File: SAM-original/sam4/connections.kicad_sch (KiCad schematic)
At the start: 24 parts, among them J10 Conn_01x02_Socket, J11 Conn_01x02_Socket, J12 10103594-0001LF, J13 Conn_01x04_Socket, J14 Conn_01x04_Socket, J15 Conn_01x04_Socket, J16 Conn_01x04_Socket, J17 Conn_01x04_Socket, J6 XT60PW-M, J7 XT60PW-M, J8 XT30PW-F, J9 Conn_02x16_Odd_Even, SW1 SW_SPST

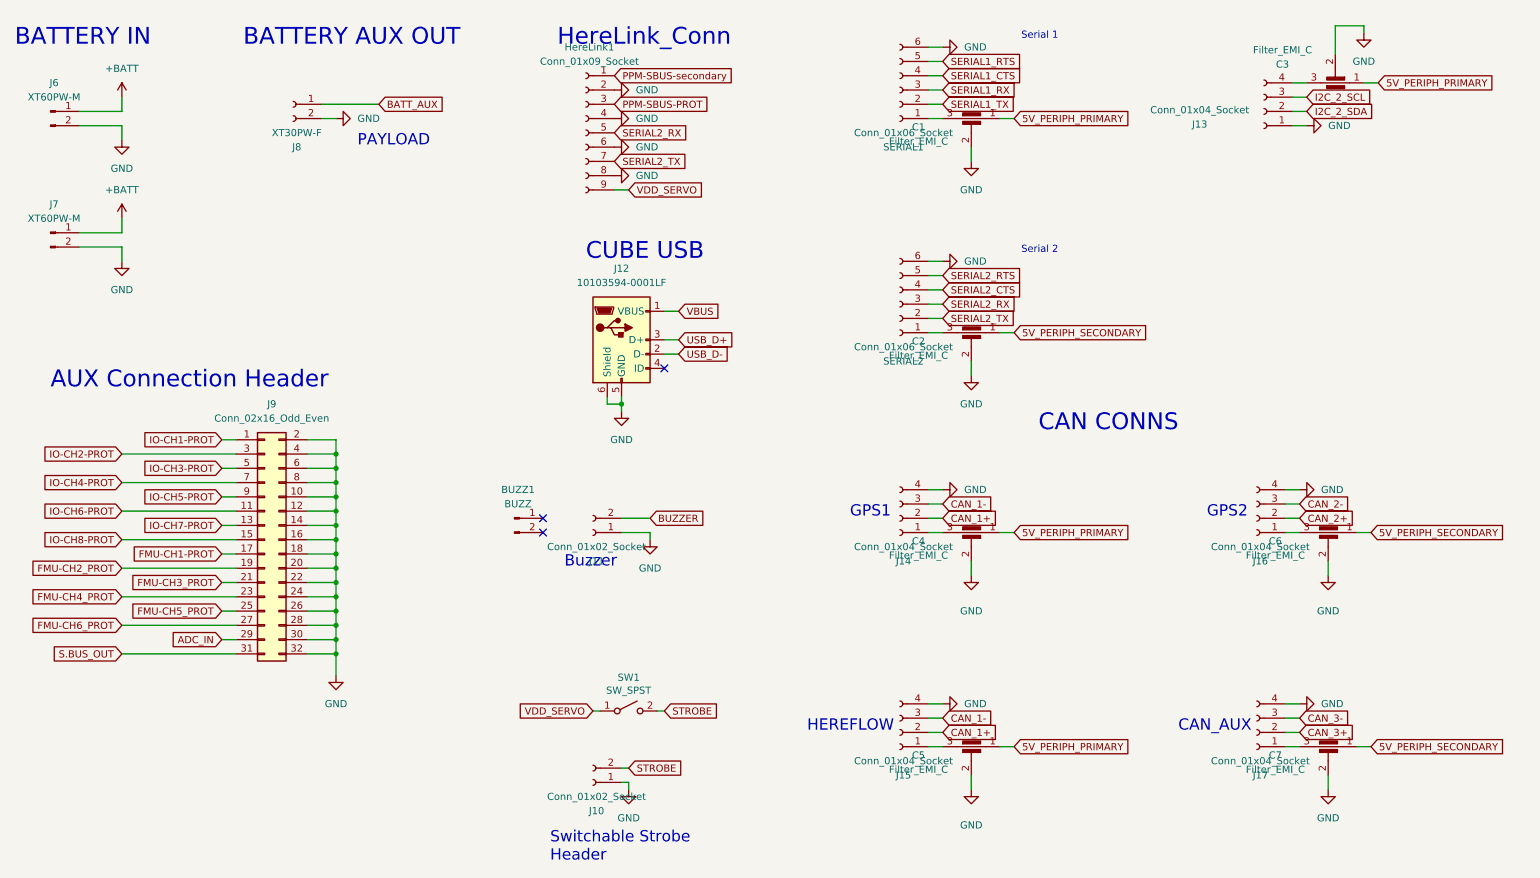
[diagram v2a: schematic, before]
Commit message: finalize core routing
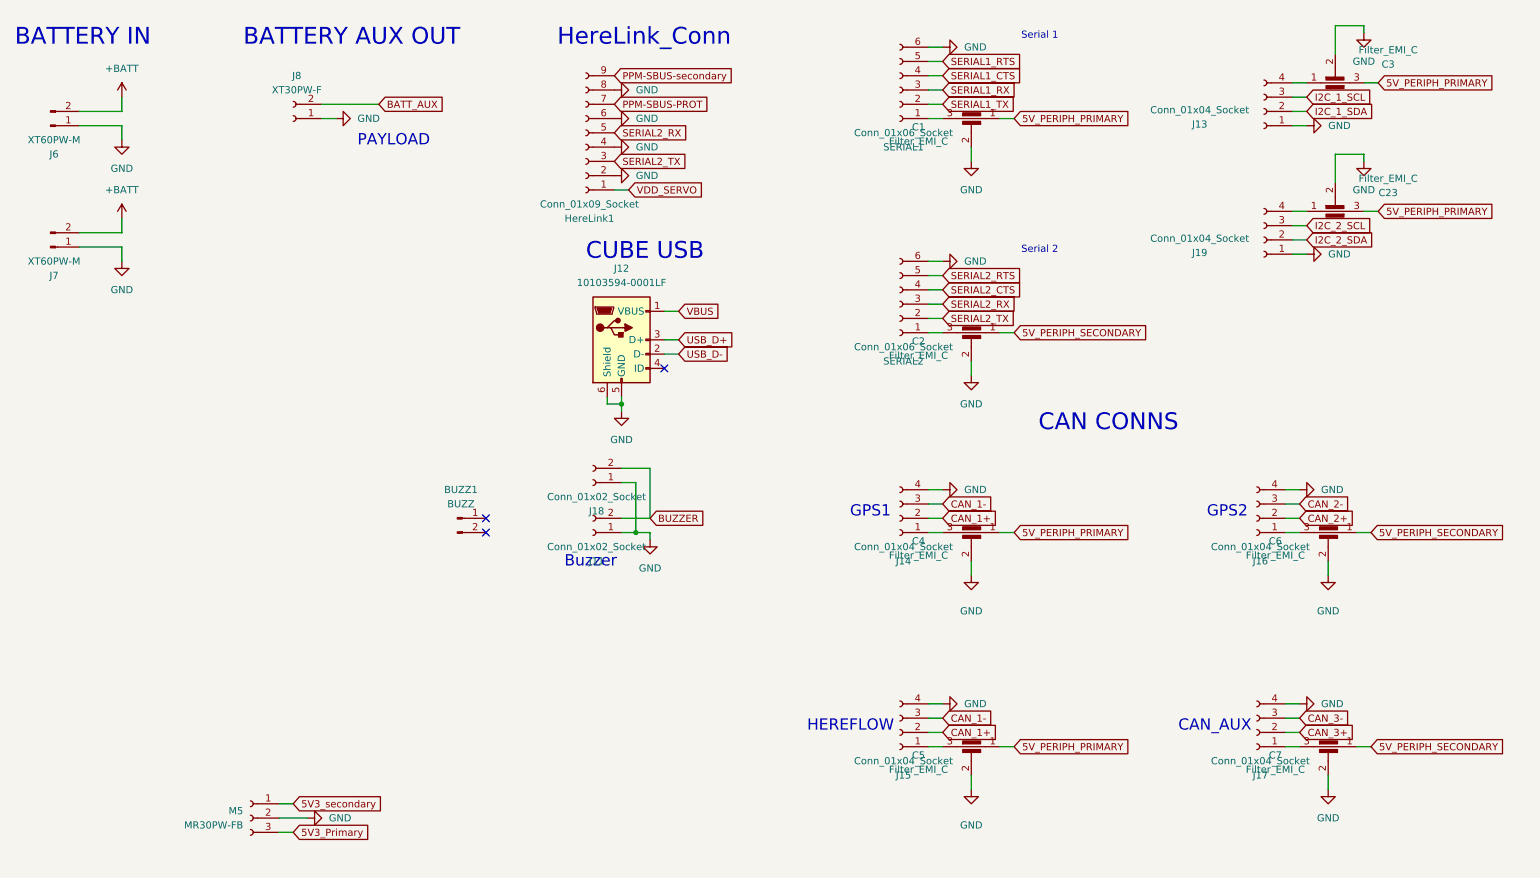
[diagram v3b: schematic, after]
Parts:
- removed J10: Conn_01x02_Socket, Connector_Molex:Molex_CLIK-Mate_502386-0270_1x02-1MP_P1.25mm_Horizontal, symbol Connector:Conn_01x02_Socket
- removed J9: Conn_02x16_Odd_Even, Connector_PinHeader_2.54mm:PinHeader_2x16_P2.54mm_Vertical, symbol Connector_Generic:Conn_02x16_Odd_Even
- removed SW1: SW_SPST, aerpaw-footprints:sam_slide_switch_5x5, symbol Switch:SW_SPST
- added C23: Filter_EMI_C, aerpaw-footprints:FIL_NFM21HC224R1A3D, symbol Device:Filter_EMI_C
- added J18: Conn_01x02_Socket, Connector_Molex:Molex_CLIK-Mate_502386-0270_1x02-1MP_P1.25mm_Horizontal, symbol Connector:Conn_01x02_Socket
- added J19: Conn_01x04_Socket, Connector_JST:JST_GH_BM04B-GHS-TBT_1x04-1MP_P1.25mm_Vertical, symbol Connector:Conn_01x04_Socket
- added M5: MR30PW-FB, Connector_AMASS:AMASS_MR30PW-FB_1x03_P3.50mm_Horizontal, symbol Connector:Conn_01x03_Socket
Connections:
- net +BATT: now also J6.2 (Pin_2), J7.2 (Pin_2); no longer J6.1 (Pin_1), J7.1 (Pin_1)
- net 5V_PERIPH_PRIMARY: now also C3.3, C23.3; no longer C3.1
- net BATT_AUX: now also J8.2 (Pin_2); no longer J8.1 (Pin_1)
- net BUZZER: now also J18.2 (Pin_2)
- net GND: now also J6.1 (Pin_1), J7.1 (Pin_1), J8.1 (Pin_1), C23.2, J18.1 (Pin_1), J19.1 (Pin_1), M5.2 (Pin_2); no longer J6.2 (Pin_2), J7.2 (Pin_2), J8.2 (Pin_2)
- net I2C_2_SCL: now also J19.3 (Pin_3); no longer J13.3 (Pin_3)
- net I2C_2_SDA: now also J19.2 (Pin_2); no longer J13.2 (Pin_2)
- net PPM-SBUS-PROT: now also HereLink1.7 (Pin_7); no longer HereLink1.3 (Pin_3)
- net PPM-SBUS-secondary: now also HereLink1.9 (Pin_9); no longer HereLink1.1 (Pin_1)
- net SERIAL2_TX: now also HereLink1.3 (Pin_3); no longer HereLink1.7 (Pin_7)
- net VDD_SERVO: now also HereLink1.1 (Pin_1); no longer HereLink1.9 (Pin_9)
- net at J13.4 (Pin_4): now also C3.1; no longer C3.3
- new net: C23.1, J19.4 (Pin_4)
- new net 5V3_Primary: M5.3 (Pin_3)
- new net 5V3_secondary: M5.1 (Pin_1)
- new net I2C_1_SCL: J13.3 (Pin_3)
- new net I2C_1_SDA: J13.2 (Pin_2)
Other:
- note removed: "AUX Connection Header"
- note removed: "Switchable Strobe Header"
- moved on the sheet: BUZZ1, C3, HereLink1, J8

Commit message: add updated SAM4 routing (DRC clean) + model
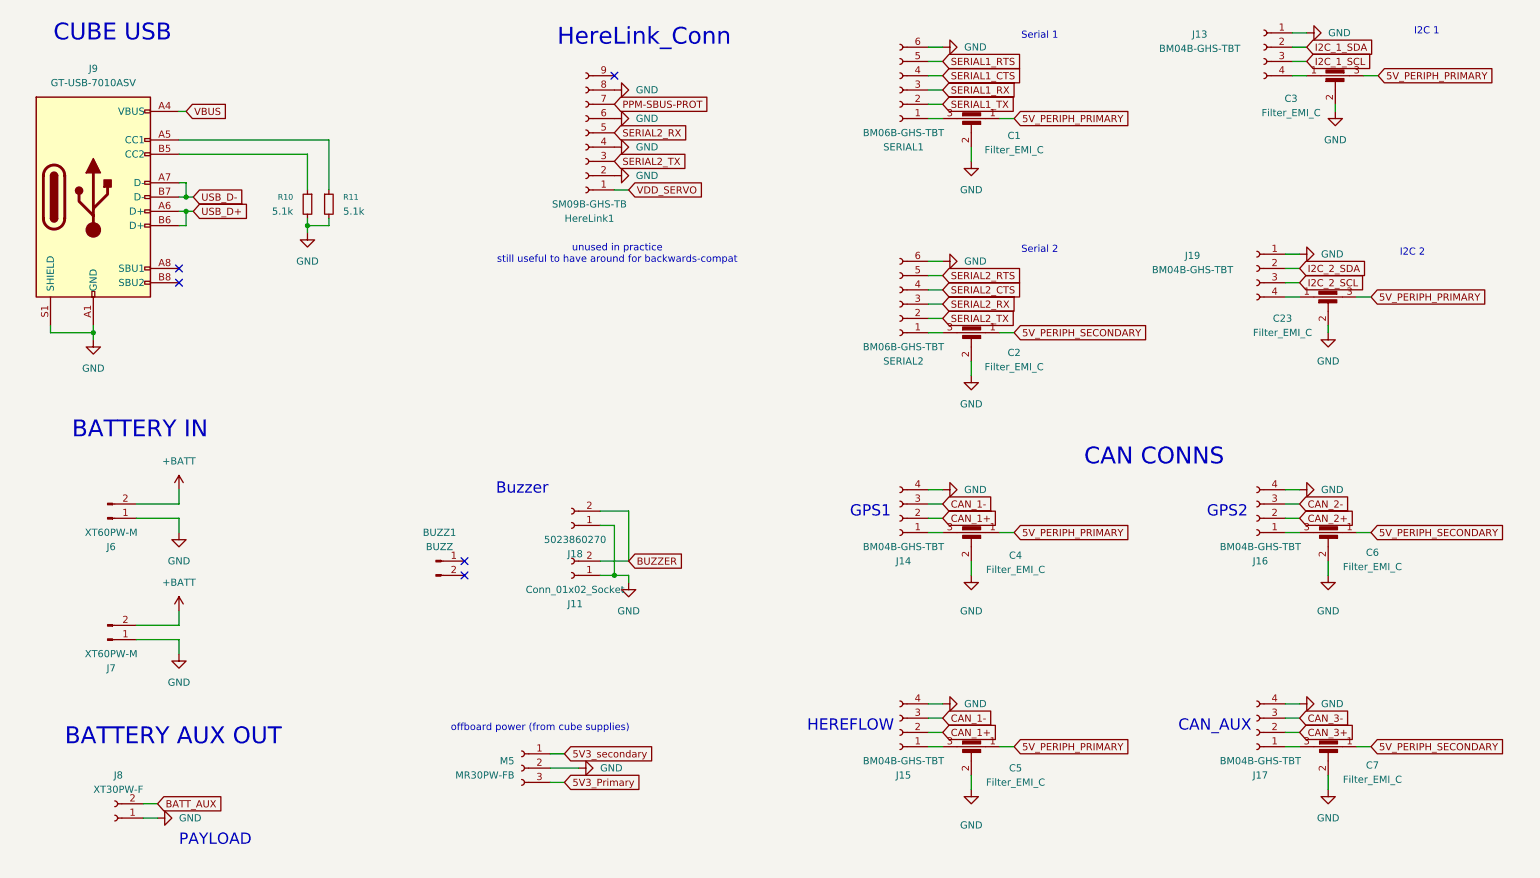
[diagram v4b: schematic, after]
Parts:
- removed J12: 10103594-0001LF, Connector_USB:USB_Micro-B_Amphenol_10103594-0001LF_Horizontal, symbol Connector:USB_B_Micro
- added J9: GT-USB-7010ASV, Connector_USB:USB_C_Receptacle_G-Switch_GT-USB-7010ASV, symbol Connector:USB_C_Receptacle_USB2.0_16P
- added R10, R11: 5.1k, Resistor_SMD:R_0805_2012Metric_Pad1.20x1.40mm_HandSolder, symbol Device:R_Small
- C1, C2, C23, C3, C4, C5, C6, C7: LCSC (none) -> C6123199
- HereLink1: value Conn_01x09_Socket -> SM09B-GHS-TB; LCSC (none) -> C265420
- J13, J14, J15, J16, J17, J19: value Conn_01x04_Socket -> BM04B-GHS-TBT; LCSC (none) -> C161692
- J18: value Conn_01x02_Socket -> 5023860270; LCSC (none) -> C2961157
- J6, J7: LCSC (none) -> C98732
- J8: LCSC (none) -> C2913282
- M5: LCSC (none) -> C19268035
- SERIAL1, SERIAL2: value Conn_01x06_Socket -> BM06B-GHS-TBT; LCSC (none) -> C485353
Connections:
- net GND: now also J9.A1 (GND), J9.A12 (GND), J9.B1 (GND), J9.B12 (GND), J9.S1 (SHIELD), R10.2, R11.2
- net USB_D+: now also J9.A6 (D+), J9.B6 (D+)
- net USB_D-: now also J9.A7 (D-), J9.B7 (D-)
- net VBUS: now also J9.A4 (VBUS), J9.A9 (VBUS), J9.B4 (VBUS), J9.B9 (VBUS)
- net PPM-SBUS-secondary: no longer names the net of HereLink1.9 (Pin_9)
- new net: J9.A5 (CC1), R11.1
- new net: J9.B5 (CC2), R10.1
- no-connect marks 3 -> 5
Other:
- note added: "I2C 1"
- note added: "I2C 2"
- note added: "offboard power (from cube supplies)"
- note added: "unused in practice still useful to have around for backwards-compat"
- moved on the sheet: BUZZ1, C23, C3, J11, J13, J18, J19, J6, J7, J8, M5
